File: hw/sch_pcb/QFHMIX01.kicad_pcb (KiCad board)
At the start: 2 copper layers, 90.9 x 90.9 mm, 205 parts, among them J1 HEADER_1x08, J2 +9V, M1 HOLE, M2 HOLE, M3 HOLE, M4 HOLE, M5 HOLE, M6 HOLE, M7 HOLE, M8 HOLE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

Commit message: Edit PCB
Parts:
- moved C30 12.5 mm to (151.9, 80.7), turned to 45 degrees
- moved C29 12.5 mm to (148.9, 77.7), turned to 45 degrees
- moved C68 11.0 mm to (165.7, 115.7)
- moved L63 9.97 mm to (154.9, 79.1)
- moved C70 7.46 mm to (167.1, 117.2)
- moved L69 7.18 mm to (152.0, 76.0), turned to -135 degrees
- moved L67 4.04 mm to (156.5, 76.6), turned to -45 degrees
- moved L65 3.61 mm to (158.9, 71.6)
- moved L59 3.28 mm to (153.3, 64.5)
- moved R37 2.85 mm to (155.6, 62.6)
- moved C58 2.71 mm to (152.3, 67.1)
- moved L22 2.61 mm to (153.2, 60.5)
- moved C43 2.53 mm to (156.9, 61.9)
- moved L60 2.52 mm to (152.3, 70.5)
- moved L39 2.46 mm to (154.3, 73.5), turned to -90 degrees
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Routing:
- net VCC: track 13.2 -> 88.5 mm, vias 1 -> 4
- net +5V: track 95.5 -> 150.9 mm, vias 18 -> 13
- net Net-(C67-Pad2): track 0.00 -> 43.2 mm, vias 1 -> 0
- net Net-(C74-Pad2): track 0.00 -> 17.6 mm, vias 1 -> 0
- net Net-(C72-Pad1): track 0.00 -> 8.60 mm
- net Net-(R48-Pad2): track 0.00 -> 4.79 mm
- net Net-(C7-Pad1): track 0.00 -> 4.39 mm
- net Net-(C5-Pad1): track 0.00 -> 4.06 mm
- net Net-(C6-Pad1): track 0.00 -> 3.82 mm
- net Net-(C4-Pad1): track 0.00 -> 3.49 mm, vias 1 -> 0
- net Net-(D3-Pad2): track 0.00 -> 2.25 mm
- net Net-(C72-Pad2): track 0.00 -> 1.87 mm, vias 1 -> 0
- net GND: track 48.9 -> 47.2 mm, vias 296 -> 290
- net +3V3: track 85.5 -> 87.2 mm
- net Net-(L22-Pad2): track 1.63 -> 0.00 mm
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
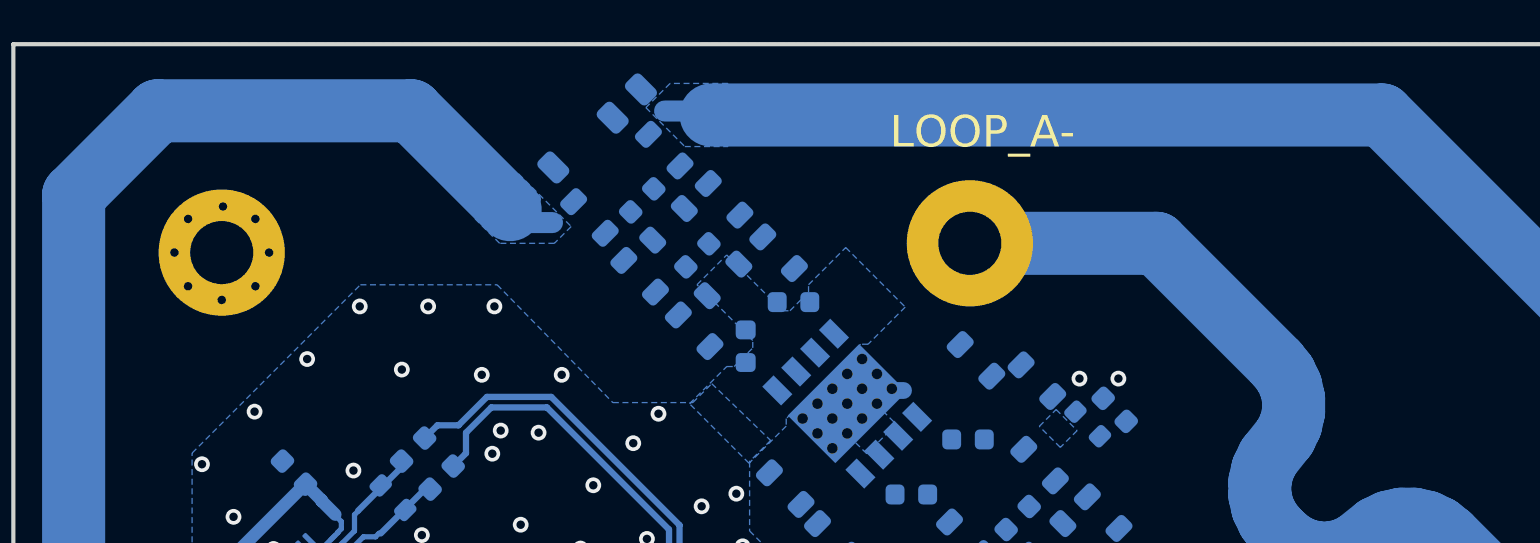
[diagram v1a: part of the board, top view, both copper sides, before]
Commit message: RF filter layout improvement.
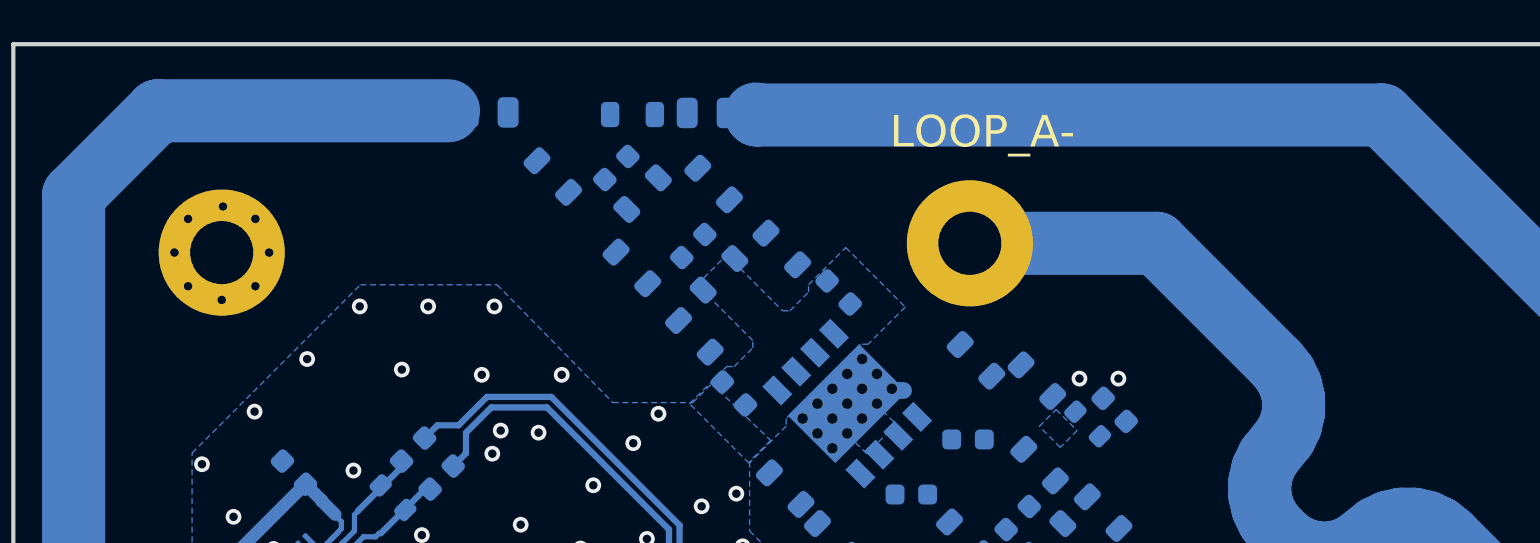
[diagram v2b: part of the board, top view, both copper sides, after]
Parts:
- moved C14 4.09 mm to (127.1, 47.8), turned to 180 degrees
- moved C31 3.85 mm to (137.5, 47.8), turned to 180 degrees
- moved L5 2.61 mm to (130.2, 50.8)
- moved C47 2.32 mm to (138.8, 61.1), turned to 135 degrees
- moved L14 2.27 mm to (134.0, 47.9), turned to 180 degrees
- moved C33 2.19 mm to (143.8, 56.3), turned to -45 degrees
- moved C32 1.97 mm to (133.2, 50.4)
- moved L17 1.91 mm to (134.4, 51.6)
- moved L53 0.88 mm to (137.8, 51.2)
- moved L52 0.54 mm to (133.9, 55.2)
- moved C45 0.48 mm to (136.9, 54.1)
- moved L54 0.33 mm to (138.1, 55.5)
- moved L55 0.26 mm to (136.9, 58.4)
- moved L56 0.23 mm to (141.1, 54.3)
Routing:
- net /LNA/QFH_IN_1_P: track 82.8 -> 76.0 mm
- net /LNA/QFH_IN_1_N: track 83.2 -> 78.8 mm
- removed copper zone on B.Cu, net /LNA/QFH_IN_1_N
- removed copper zone on B.Cu, net /LNA/QFH_IN_1_P

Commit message: RF layout.
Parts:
- moved C65 3.76 mm to (154.6, 76.4), turned to 135 degrees
- moved L67 3.65 mm to (152.9, 77.1)
- moved L65 3.48 mm to (158.3, 75.1), turned to 45 degrees
- moved L69 2.77 mm to (149.6, 77.4)
- moved L18 2.28 mm to (141.8, 69.6)
- moved L19 2.14 mm to (143.1, 66.8), turned to 45 degrees
- moved C29 2.11 mm to (146.8, 77.8)
- moved C63 1.98 mm to (156.8, 70.1)
- moved L36 1.80 mm to (158.0, 71.3)
- moved C30 1.78 mm to (151.8, 82.5)
- moved L60 1.66 mm to (153.9, 70.8)
- moved C49 1.60 mm to (146.2, 67.2), turned to 135 degrees
- moved L39 1.58 mm to (155.8, 74.1), turned to -135 degrees
- moved L63 1.41 mm to (153.8, 80.0)
- moved L58 1.40 mm to (148.6, 67.3)
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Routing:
- net Net-(L18-Pad1): vias 0 -> 1
- net GND: vias 290 -> 289

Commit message: Edit PCB
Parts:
- C66, C67: footprint Mlab_C:SMD-0603 -> Capacitor_SMD:C_0603_1608Metric
- C69: value 10uF -> 10uF/16
- R12, R27, R28, R29, R30: value 100 -> 100R
- R31, R32, R33, R34: value 50 -> 49R9
- R35, R36, R37, R38, R39, R40, R41, R42: value 3 -> 3R
- U1: value LM1117MP-3,3/NO -> NCP1117ST33
- moved L68 10.1 mm to (159.6, 87.8), turned to -135 degrees
- moved L70 5.76 mm to (162.4, 90.4), turned to 45 degrees
- moved C39 5.21 mm to (192.4, 109.8), turned to 90 degrees
- moved L37 5.15 mm to (164.3, 82.3), turned to -135 degrees
- moved C34 4.81 mm to (192.4, 100.1), turned to 90 degrees
- moved L66 4.28 mm to (162.8, 86.8), turned to -45 degrees
- moved L21 4.03 mm to (170.0, 96.8)
- moved L25 4.00 mm to (179.8, 87.3)
- moved L35 3.90 mm to (169.7, 82.6)
- moved R36 3.41 mm to (167.2, 94.2)
- moved L15 3.31 mm to (192.4, 103.8), turned to -90 degrees
- moved C40 3.26 mm to (189.8, 105.7)
- moved L16 3.11 mm to (188.6, 108.5)
- moved L31 3.00 mm to (173.1, 83.3)
- moved L62 2.95 mm to (188.5, 104.6)
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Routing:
- net +5V: track 150.9 -> 207.6 mm, vias 13 -> 16
- net Net-(C52-Pad2): track 0.00 -> 10.1 mm
- net Net-(C63-Pad1): track 0.00 -> 7.40 mm
- net Net-(C51-Pad1): track 0.00 -> 7.29 mm
- net Net-(C40-Pad2): track 0.00 -> 7.00 mm
- net Net-(C51-Pad2): track 0.00 -> 6.99 mm
- net /LNA/QFH_IN_2_P: track 83.2 -> 76.4 mm
- net Net-(C65-Pad1): track 0.00 -> 6.54 mm
- net Net-(C45-Pad2): track 0.00 -> 6.51 mm
- net Net-(C45-Pad1): track 0.00 -> 6.42 mm
- net Net-(C52-Pad1): track 0.00 -> 6.42 mm
- net Net-(C46-Pad2): track 0.00 -> 6.34 mm
- net Net-(C32-Pad2): track 0.00 -> 6.28 mm
- net Net-(C32-Pad1): track 0.00 -> 6.07 mm
- net Net-(C46-Pad1): track 0.00 -> 5.93 mm
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- removed copper zone on B.Cu, net /LNA/QFH_IN_2_N
- removed copper zone on B.Cu, net /LNA/QFH_IN_2_P

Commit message: Edit PCB
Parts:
- moved L22 0.28 mm to (153.0, 60.5)
- moved C22 0.25 mm to (142.9, 108.7)
- moved R40 0.18 mm to (162.9, 96.4)
- moved R39 0.18 mm to (143.6, 77.1)
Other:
- board text added: "QFHMIX01D"
- board text added: "mlab.cz 2021"
- board text removed: "QFHMIX01"

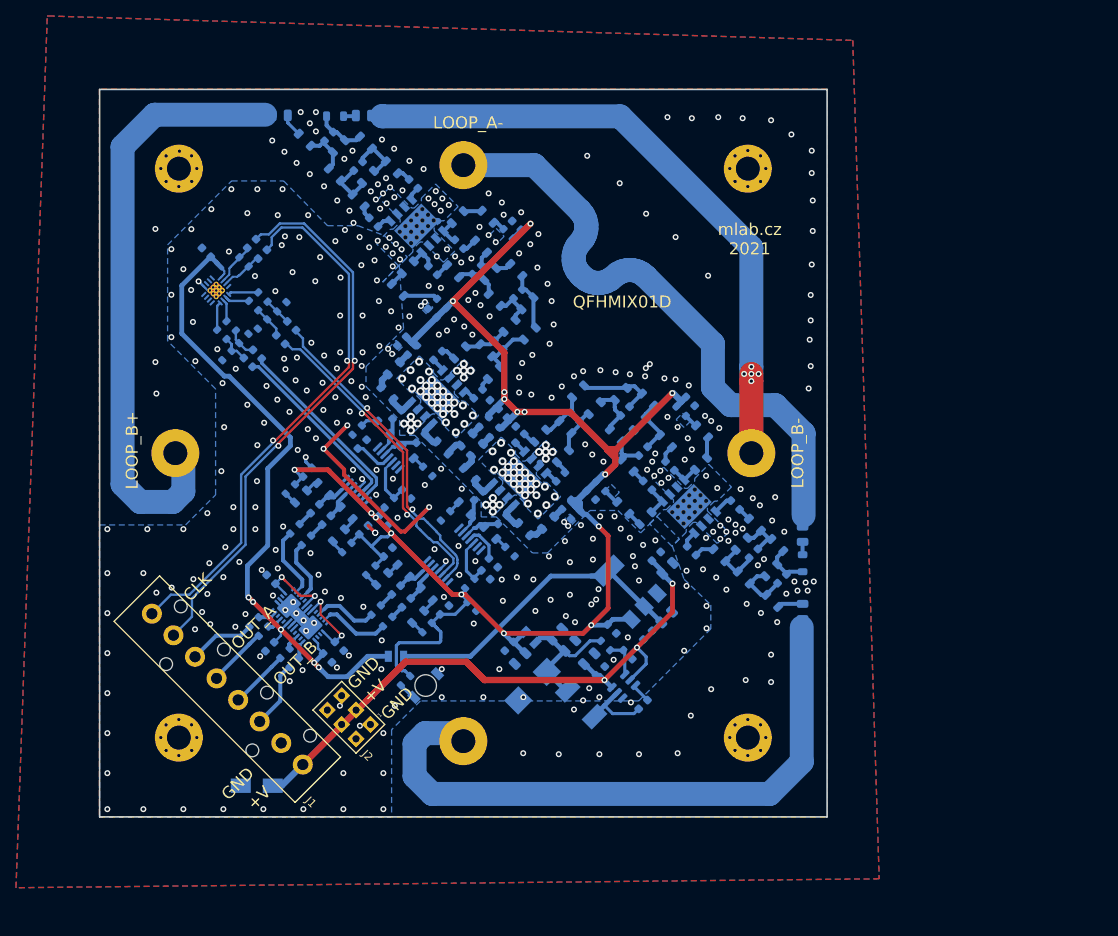
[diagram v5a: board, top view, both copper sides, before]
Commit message: Switching regulator layout improvement.
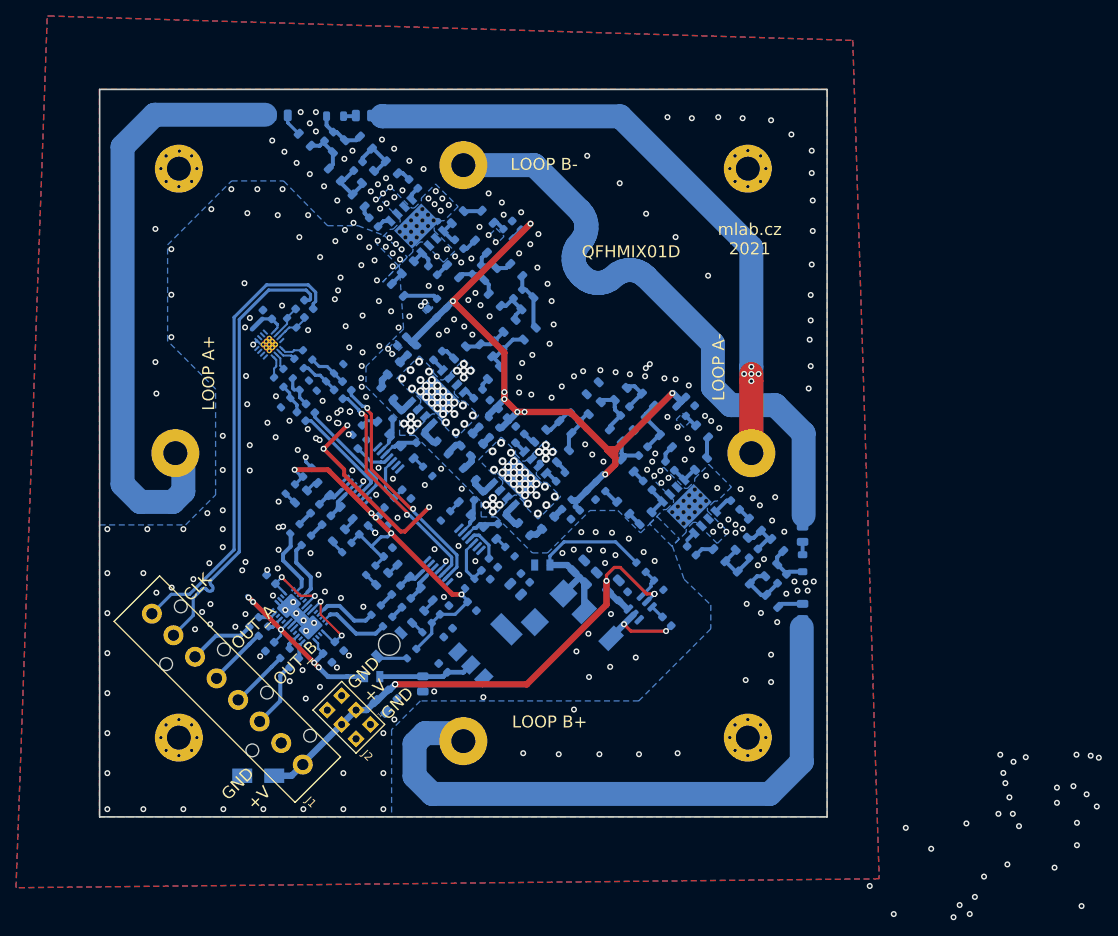
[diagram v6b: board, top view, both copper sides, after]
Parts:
- moved C27 39.8 mm to (139.7, 121.7), turned to -45 degrees
- moved C28 37.2 mm to (141.1, 120.1), turned to -45 degrees
- moved C69 31.6 mm to (144.9, 118.8), turned to -90 degrees
- moved C67 25.9 mm to (147.5, 116.8), turned to -45 degrees
- moved C66 20.5 mm to (148.1, 112.4), turned to 45 degrees
- moved U1 18.7 mm to (153.2, 114.2), turned to 45 degrees
- moved C3 10.9 mm to (125.5, 72.7)
- moved C72 10.8 mm to (175.4, 111.0), turned to 135 degrees
- moved R52 10.7 mm to (172.2, 104.3)
- moved R7 10.7 mm to (132.3, 81.6)
- moved R4 10.5 mm to (134.4, 79.5)
- moved C4 10.2 mm to (135.4, 81.6)
- moved C76 10.0 mm to (164.4, 104.1)
- moved L49 10.0 mm to (166.8, 111.5)
- moved U11 10.0 mm to (172.1, 109.4)
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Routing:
- net +5V: track 207.5 -> 146.9 mm, vias 16 -> 13
- net +3V3: track 87.2 -> 33.0 mm
- net Net-(C67-Pad2): track 43.2 -> 12.0 mm
- net VCC: track 88.5 -> 68.0 mm, vias 3 -> 7
- net CLK_IN_P: track 70.9 -> 57.0 mm, vias 2 -> 0
- net CLK_IN_N: track 68.8 -> 57.1 mm, vias 2 -> 0
- net /CLK_MIX1_P: track 24.6 -> 13.5 mm
- net /CLK_MIX2_P: track 39.3 -> 28.4 mm
- net /CLK_MIX2_N: track 40.1 -> 29.5 mm
- net /CLK_MIX1_N: track 24.2 -> 14.5 mm
- net Net-(C74-Pad2): track 17.6 -> 26.4 mm
- net Net-(C52-Pad2): track 10.1 -> 4.65 mm
- net Net-(C64-Pad2): track 5.90 -> 4.18 mm
- net Net-(C72-Pad1): track 9.10 -> 10.7 mm, vias 0 -> 2
- net Net-(D3-Pad2): track 2.25 -> 3.79 mm
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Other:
- board text added: "LOOP A+"
- board text added: "LOOP A-"
- board text added: "LOOP B+"
- board text added: "LOOP B-"
- board text removed: "LOOP_A-"
- board text removed: "LOOP_B+"
- board text removed: "LOOP_B-"

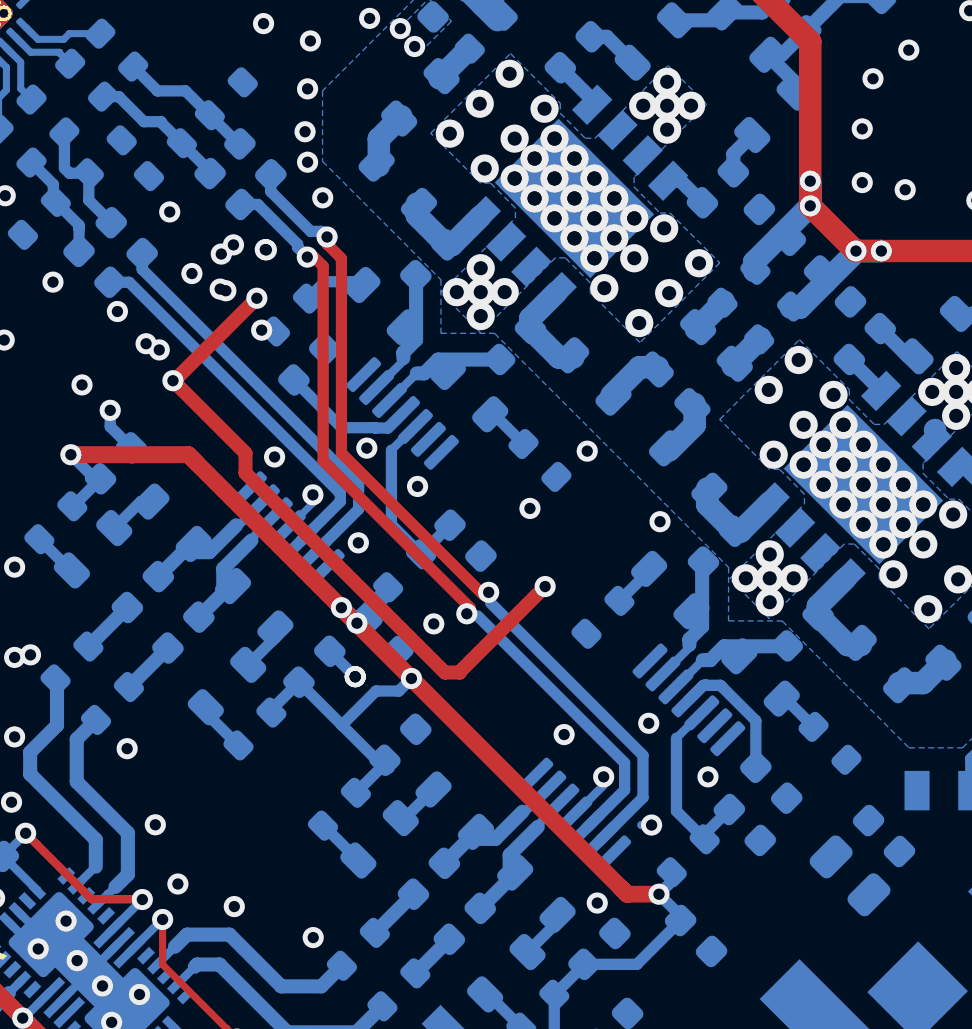
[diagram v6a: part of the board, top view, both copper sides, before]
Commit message: Eliminate vias on RF LO tracks.
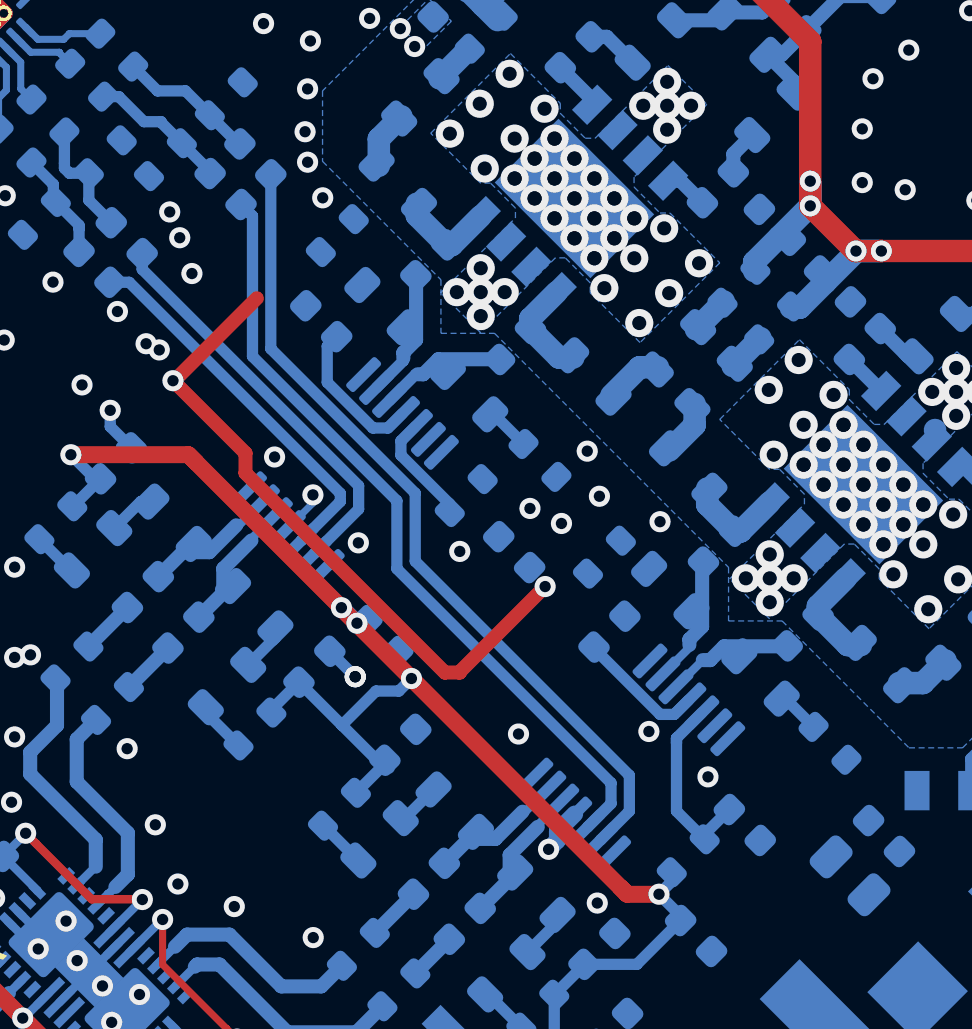
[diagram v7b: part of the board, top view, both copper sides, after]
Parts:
- moved C13 7.85 mm to (148.0, 98.3), turned to 45 degrees
- moved R9 3.45 mm to (142.9, 93.5), turned to -135 degrees
- moved R2 3.25 mm to (138.4, 84.3), turned to 45 degrees
- moved R3 2.14 mm to (147.8, 95.7)
- moved C10 1.77 mm to (144.6, 95.5)
- moved C12 1.59 mm to (137.8, 87.3), turned to 135 degrees
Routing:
- net Net-(C10-Pad1): track 6.72 -> 3.98 mm
- net Net-(C13-Pad1): track 7.07 -> 4.59 mm
- net Net-(L2-Pad1): track 2.06 -> 0.00 mm
- net +5V: track 146.9 -> 145.4 mm
- net Net-(L3-Pad1): track 1.57 -> 0.08 mm
- net Net-(C11-Pad1): track 6.63 -> 8.08 mm
- net /LNA/LNA_OUT_1_P: track 4.62 -> 6.05 mm
- net /LNA/LNA_OUT_1_N: track 4.67 -> 6.01 mm
- net Net-(C12-Pad1): track 4.77 -> 5.31 mm
- net /CLK_MIX2_P: track 28.4 -> 27.9 mm, vias 2 -> 0
- net /CLK_MIX2_N: track 29.5 -> 29.3 mm, vias 2 -> 0
- net GND: track 42.1 -> 42.3 mm, vias 476 -> 468
